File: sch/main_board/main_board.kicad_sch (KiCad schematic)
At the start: 58 parts, among them J1 BVCC, J13 5V_GND, J14 IO23, J15 IO22, J16 IO1, J17 IO3, J18 IO21, J19 IO19, J2 BGND, J21 5V, J22 TX2, J23 RX2, J24 12V_CUT2, J25 12V_CUT, J26 DC 12V, J27 DC 5V, J3 3.3V, J30 5V_CUT, J4 PWR_MOTOR_L, J5 PWR_MOTOR_R, J6 CUT_LOAD, J7 MOTOR_L, J8 MOTOR_R, J9 EN, Q1 BC847, Q2 K4145, Q3 K4145, Q4 BC847, Q5 K4145, Q6 BC847, Q7 K4145, Q8 BC847, Q9 K4145

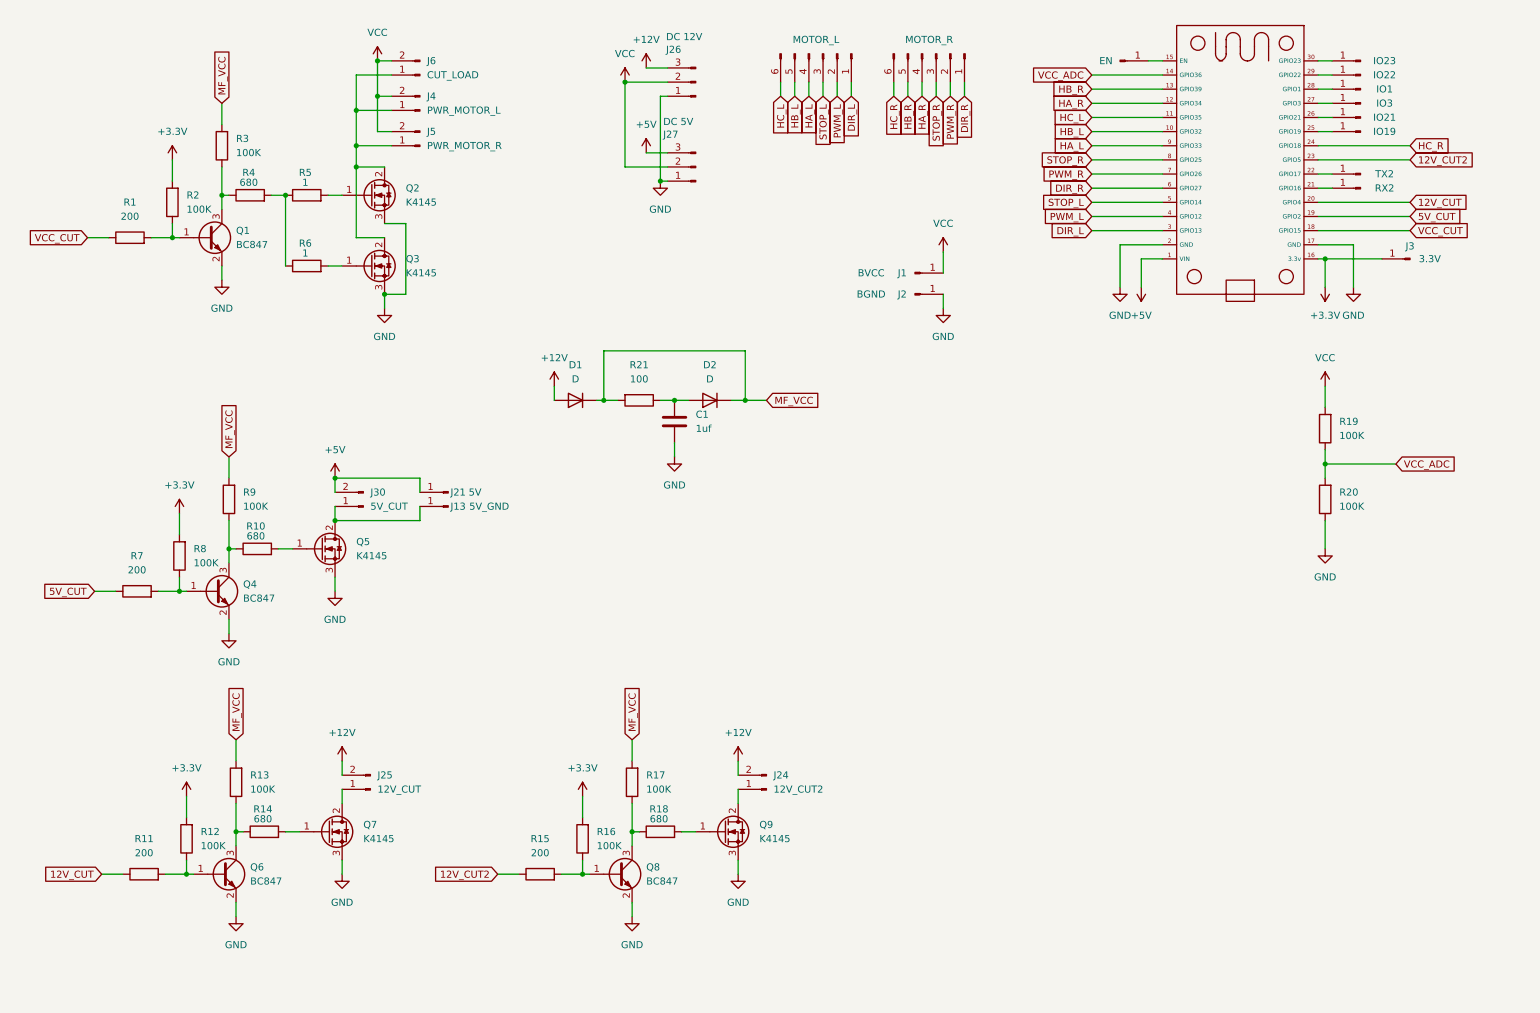
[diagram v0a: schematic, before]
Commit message: 1. Reconnect 5V_CUT from GPIO2 to GPIO19. Because GPIO2 is the LED 2. Pull-up RX2 3. Figured out with VCC_ADC resistor divider 4. Change input to NPN cut transistor from 200 Om to 10K. 200 Om is way to small value which eats a lot of current.
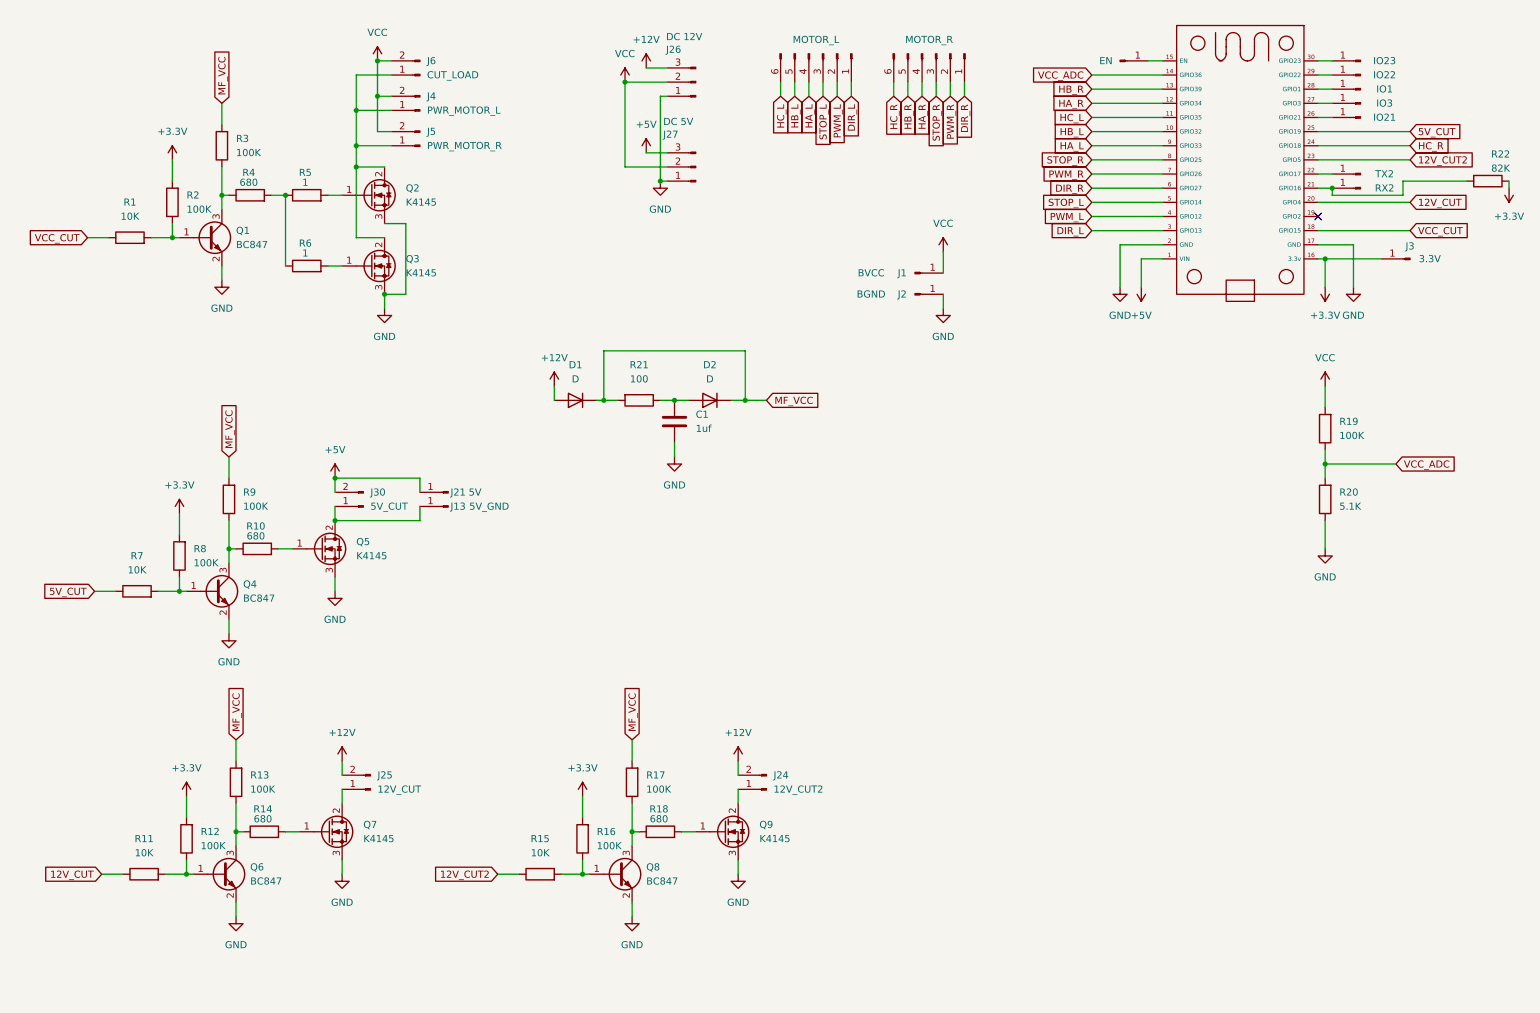
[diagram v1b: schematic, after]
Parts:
- removed J19: IO19, Connector_Wire:SolderWirePad_1x01_SMD_1.5x3mm, symbol Connector:Conn_01x01_Pin
- added R22: 82K, Resistor_SMD:R_0805_2012Metric, symbol Device:R
- R1, R11, R15, R7: value 200 -> 10K
- R20: value 100K -> 5.1K
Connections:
- net +3.3V: now also R22.1
- net 5V_CUT: now also U1.25 (GPIO19); no longer U1.19 (GPIO2)
- net at J23.1 (Pin_1), U1.21 (GPIO16): now also R22.2
- no-connect marks 0 -> 1
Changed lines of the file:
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@@
 	)
 	(junction
+		(at 248.92 44.45)
+		(diameter 0)
+		(color 0 0 0 0)
+	)
+	(junction
 		(at 118.11 82.55)
 		(diameter 0)
@@
 		(color 0 0 0 0)
 	)
+	(no_connect
+		(at 246.38 49.53)
+	)
 	(wire
 		(pts
@@
 	(wire
 		(pts
+			(xy 261.62 45.72) (xy 248.92 45.72)
+		)
+		(stroke
+			(width 0)
+			(type default)
+		)
+	)
+	(wire
+		(pts
+			(xy 261.62 43.18) (xy 261.62 45.72)
+		)
+		(stroke
+			(width 0)
+			(type default)
+		)
+	)
+	(wire
+		(pts
 			(xy 77.47 34.29) (xy 80.01 34.29)
 		)
@@
 	(wire
 		(pts
+			(xy 273.05 43.18) (xy 261.62 43.18)
+		)
+		(stroke
+			(width 0)
+			(type default)
+		)
+	)
+	(wire
+		(pts
 			(xy 128.27 43.18) (xy 129.54 43.18)
 		)
@@
 	(wire
 		(pts
+			(xy 246.38 34.29) (xy 262.89 34.29)
+		)
+		(stroke
+			(width 0)
+			(type default)
+		)
+	)
+	(wire
+		(pts
 			(xy 140.97 82.55) (xy 143.51 82.55)
 		)
@@
 	(wire
 		(pts
-			(xy 246.38 34.29) (xy 248.92 34.29)
+			(xy 143.51 82.55) (xy 147.32 82.55)
 		)
 		(stroke
@@
 	(wire
 		(pts
-			(xy 143.51 82.55) (xy 147.32 82.55)
+			(xy 248.92 44.45) (xy 248.92 45.72)
 		)
 		(stroke
@@
 	(wire
 		(pts
-			(xy 246.38 49.53) (xy 262.89 49.53)
-		)
-		(stroke
-			(width 0)
-			(type default)
-		)
-	)
-	(wire
-		(pts
 			(xy 52.07 154.94) (xy 52.07 160.02)
 		)
@@
 	(wire
 		(pts
+			(xy 280.67 43.18) (xy 280.67 44.45)
+		)
+		(stroke
+			(width 0)
+			(type default)
+		)
+	)
+	(wire
+		(pts
 			(xy 246.38 26.67) (xy 248.92 26.67)
 		)
@@
 	(global_label "5V_CUT"
 		(shape input)
-		(at 262.89 49.53 0)
+		(at 262.89 34.29 0)
 		(fields_autoplaced yes)
 		(effects
@@
 		)
 		(property "Intersheetrefs" "${INTERSHEET_REFS}"
-			(at 272.709 49.53 0)
+			(at 272.709 34.29 0)
 			(effects
 				(font
@@
 			)
 		)
-		(property "Value" "200"
+		(property "Value" "10K"
 			(at 34.29 113.03 90)
 			(effects
@@
 	)
 	(symbol
-		(lib_id "Connector:Conn_01x01_Pin")
-		(at 254 34.29 180)
+		(lib_id "power:+12V")
+		(at 142.24 147.32 0)
 		(unit 1)
 		(exclude_from_sim no)
@@
 		(on_board yes)
 		(dnp no)
-		(property "Reference" "J19"
-			(at 256.794 34.29 0)
+		(fields_autoplaced yes)
+		(property "Reference" "#PWR020"
+			(at 142.24 151.13 0)
 			(effects
 				(font
@@
 			)
 		)
-		(property "Value" "IO19"
-			(at 258.318 34.29 0)
+		(property "Value" "+12V"
+			(at 142.24 142.24 0)
 			(effects
 				(font
@@
 			)
 		)
-		(property "Footprint" "Connector_Wire:SolderWirePad_1x01_SMD_1.5x3mm"
-			(at 254 34.29 0)
+		(property "Footprint" ""
+			(at 142.24 147.32 0)
 			(effects
 				(font
@@
 			)
 		)
-		(property "Datasheet" "~"
-			(at 254 34.29 0)
+		(property "Datasheet" ""
+			(at 142.24 147.32 0)
 			(effects
 				(font
@@
 			)
 		)
-		(property "Description" "Generic connector, single row, 01x01, script generated"
-			(at 254 34.29 0)
+		(property "Description" "Power symbol creates a global label with name \"+12V\""
+			(at 142.24 147.32 0)
 			(effects
 				(font
@@
 			(project "main_board"
 				(path "/5ff56e8c-d74c-48b5-bb80-16344d2bb859"
-					(reference "J19")
+					(reference "#PWR020")
 					(unit 1)
 				)
@@
 	)
 	(symbol
-		(lib_id "power:+12V")
-		(at 142.24 147.32 0)
+		(lib_id "Connector:Conn_01x02_Pin")
+		(at 85.09 24.13 180)
 		(unit 1)
 		(exclude_from_sim no)
@@
 		(dnp no)
 		(fields_autoplaced yes)
-		(property "Reference" "#PWR020"
-			(at 142.24 151.13 0)
+		(property "Reference" "J6"
+			(at 86.36 21.5899 0)
 			(effects
 				(font
 					(size 1.27 1.27)
 				)
-				(hide yes)
+				(justify right)
 			)
 		)
-		(property "Value" "+12V"
-			(at 142.24 142.24 0)
+		(property "Value" "CUT_LOAD"
+			(at 86.36 24.1299 0)
 			(effects
 				(font
 					(size 1.27 1.27)
 				)
+				(justify right)
 			)
 		)
-		(property "Footprint" ""
-			(at 142.24 147.32 0)
+		(property "Footprint" "Connector_Wire:SolderWire-2.5sqmm_1x02_P7.2mm_D2.4mm_OD3.6mm"
+			(at 85.09 24.13 0)
 			(effects
 				(font
@@
 			)
 		)
-		(property "Datasheet" ""
-			(at 142.24 147.32 0)
+		(property "Datasheet" "~"
+			(at 85.09 24.13 0)
 			(effects
 				(font
@@
 			)
 		)
-		(property "Description" "Power symbol creates a global label with name \"+12V\""
-			(at 142.24 147.32 0)
+		(property "Description" "Generic connector, single row, 01x02, script generated"
+			(at 85.09 24.13 0)
 			(effects
 				(font
@@
 		(pin "1"
 		)
+		(pin "2"
+		)
 		(instances
 			(project "main_board"
 				(path "/5ff56e8c-d74c-48b5-bb80-16344d2bb859"
-					(reference "#PWR020")
+					(reference "J6")
 					(unit 1)
 				)
@@
 	)
 	(symbol
-		(lib_id "Connector:Conn_01x02_Pin")
-		(at 85.09 24.13 180)
+		(lib_id "power:+3.3V")
+		(at 280.67 44.45 180)
 		(unit 1)
 		(exclude_from_sim no)
@@
 		(dnp no)
 		(fields_autoplaced yes)
-		(property "Reference" "J6"
-			(at 86.36 21.5899 0)
+		(property "Reference" "#PWR05"
+			(at 280.67 40.64 0)
 			(effects
 				(font
 					(size 1.27 1.27)
 				)
-				(justify right)
+				(hide yes)
 			)
 		)
-		(property "Value" "CUT_LOAD"
-			(at 86.36 24.1299 0)
+		(property "Value" "+3.3V"
+			(at 280.67 49.53 0)
 			(effects
 				(font
 					(size 1.27 1.27)
 				)
-				(justify right)
 			)
 		)
-		(property "Footprint" "Connector_Wire:SolderWire-2.5sqmm_1x02_P7.2mm_D2.4mm_OD3.6mm"
-			(at 85.09 24.13 0)
+		(property "Footprint" ""
+			(at 280.67 44.45 0)
 			(effects
 				(font
@@
 			)
 		)
-		(property "Datasheet" "~"
-			(at 85.09 24.13 0)
+		(property "Datasheet" ""
+			(at 280.67 44.45 0)
 			(effects
 				(font
@@
 			)
 		)
-		(property "Description" "Generic connector, single row, 01x02, script generated"
-			(at 85.09 24.13 0)
+		(property "Description" "Power symbol creates a global label with name \"+3.3V\""
+			(at 280.67 44.45 0)
 			(effects
 				(font
@@
 		(pin "1"
 		)
-		(pin "2"
-		)
 		(instances
 			(project "main_board"
 				(path "/5ff56e8c-d74c-48b5-bb80-16344d2bb859"
-					(reference "J6")
+					(reference "#PWR05")
 					(unit 1)
 				)
@@
 	)
 	(symbol
+		(lib_id "Device:R")
+		(at 276.86 43.18 270)
+		(unit 1)
+		(exclude_from_sim no)
+		(in_bom yes)
+		(on_board yes)
+		(dnp no)
+		(property "Reference" "R22"
+			(at 279.146 38.354 90)
+			(effects
+				(font
+					(size 1.27 1.27)
+				)
+			)
+		)
+		(property "Value" "82K"
+			(at 279.146 40.894 90)
+			(effects
+				(font
+					(size 1.27 1.27)
+				)
+			)
+		)
+		(property "Footprint" "Resistor_SMD:R_0805_2012Metric"
+			(at 276.86 41.402 90)
+			(effects
+				(font
+					(size 1.27 1.27)
+				)
+				(hide yes)
+			)
+		)
+		(property "Datasheet" "~"
+			(at 276.86 43.18 0)
+			(effects
+				(font
+					(size 1.27 1.27)
+				)
+				(hide yes)
+			)
+		)
+		(property "Description" "Resistor"
+			(at 276.86 43.18 0)
+			(effects
+				(font
+					(size 1.27 1.27)
+				)
+				(hide yes)
+			)
+		)
+		(pin "1"
+		)
+		(pin "2"
+		)
+		(instances
+			(project "main_board"
+				(path "/5ff56e8c-d74c-48b5-bb80-16344d2bb859"
+					(reference "R22")
+					(unit 1)
+				)
+			)
+		)
+	)
+	(symbol
 		(lib_id "power:+12V")
 		(at 71.12 147.32 0)
@@
 			)
 		)
-		(property "Value" "200"
+		(property "Value" "10K"
 			(at 106.68 163.83 90)
 			(effects
@@
 			)
 		)
-		(property "Value" "200"
+		(property "Value" "10K"
 			(at 33.02 49.53 90)
 			(effects
@@
 			)
 		)
-		(property "Value" "200"
+		(property "Value" "10K"
 			(at 35.56 163.83 90)
 			(effects
@@
 			)
 		)
-		(property "Value" "100K"
+		(property "Value" "5.1K"
 			(at 250.19 101.5999 0)
 			(effects
